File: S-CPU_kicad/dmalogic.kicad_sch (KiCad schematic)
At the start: 186 parts

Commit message: HDMA section seems correct after all. More notes added.
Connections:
- net ~{DMA_CHAN_RST} renamed ~{RESET_GDMA_CHAN_STOP_DMA_CHAN}
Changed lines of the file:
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@@
     (stroke (width 0) (type default))
   )
-  (wire (pts (xy 647.065 364.49) (xy 647.065 387.35))
+  (wire (pts (xy 647.065 367.665) (xy 647.065 387.35))
     (stroke (width 0) (type default))
   )
@@
     (stroke (width 0) (type default))
   )
-  (wire (pts (xy 475.615 364.49) (xy 647.065 364.49))
+  (wire (pts (xy 635.635 367.665) (xy 647.065 367.665))
     (stroke (width 0) (type default))
   )
@@
     (effects (font (size 1.27 1.27)) (justify right))
   )
-  (hierarchical_label "~{DMA_CHAN_RST}" (shape input) (at 254 44.45 180) (fields_autoplaced)
+  (hierarchical_label "~{RESET_GDMA_CHAN_STOP_DMA_CHAN}" (shape input) (at 254 44.45 180) (fields_autoplaced)
     (effects (font (size 1.27 1.27)) (justify right))
   )
@@
     (effects (font (size 1.27 1.27)) (justify right))
   )
-  (hierarchical_label "NEXT_CHAN_CLK" (shape input) (at 475.615 364.49 180) (fields_autoplaced)
+  (hierarchical_label "NEXT_CHAN_CLK" (shape input) (at 635.635 367.665 180) (fields_autoplaced)
     (effects (font (size 1.27 1.27)) (justify right))
   )

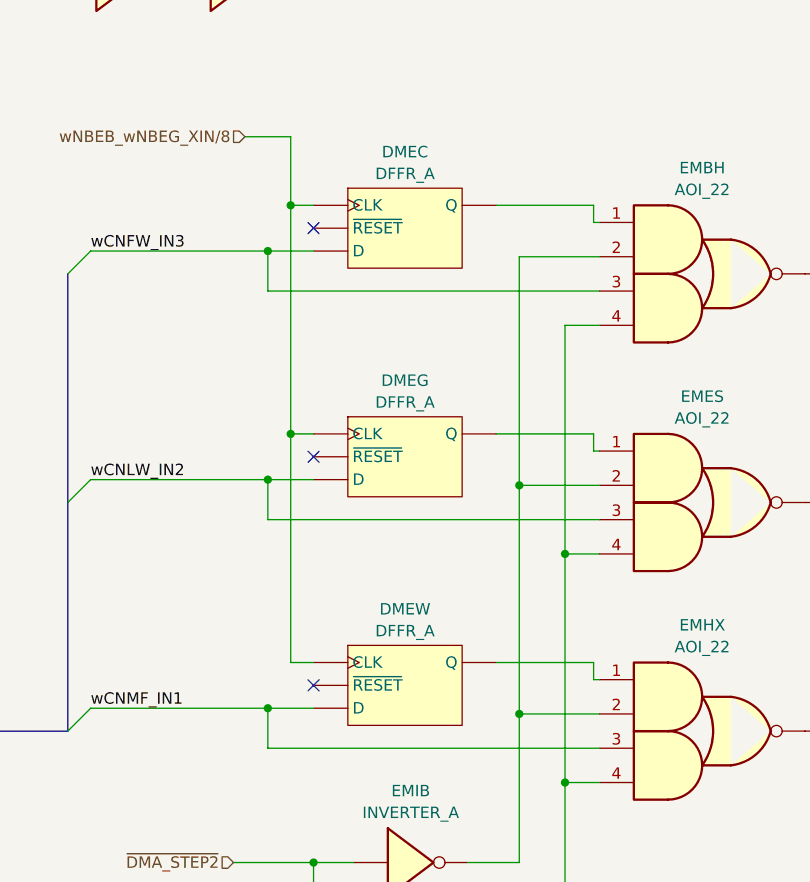
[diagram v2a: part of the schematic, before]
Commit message: Identified some DFFs as being DFFs with SET input rather than RESET input. It helps explaining a lot of beahiour in the MUL/DIV section and in the DMA section.
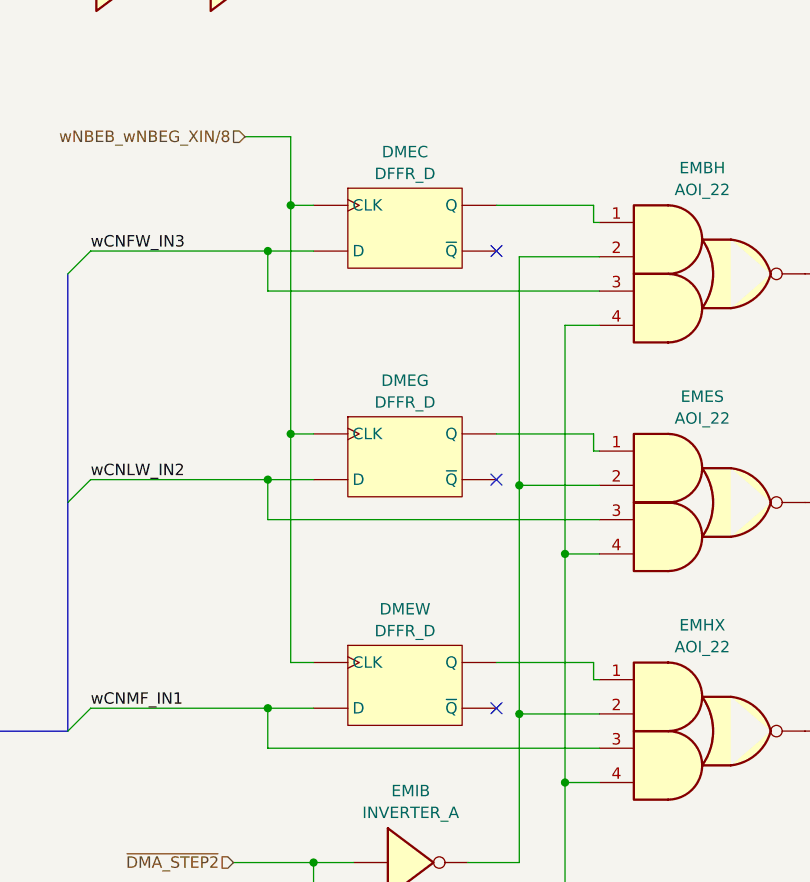
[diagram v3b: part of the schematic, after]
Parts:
- DMEC, DMEG, DMEW: value DFFR_A -> DFFR_D; symbol Ricoh_Cells:DFFR_A -> Ricoh_Cells:DFFR_D
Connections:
- net wNBEB_wNBEG_XIN/8: now also DMEC.1 (CLK), DMEG.1 (CLK), DMEW.1 (CLK); no longer DMEC.3 (CLK), DMEC.4 (~{CLK}), DMEG.3 (CLK), DMEG.4 (~{CLK}), DMEW.3 (CLK), DMEW.4 (~{CLK})
- net at EMES.1: now also DMEG.8 (Q); no longer DMEG.6 (Q)
- net at EMHX.1: now also DMEW.8 (Q); no longer DMEW.6 (Q)
- net at EMBH.1: now also DMEC.8 (Q); no longer DMEC.6 (Q)
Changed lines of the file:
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@@
   (no_connect (at 649.605 427.99))
   (no_connect (at 343.535 318.135))
-  (no_connect (at 732.79 427.99))
+  (no_connect (at 753.11 430.53))
   (no_connect (at 393.065 239.395))
   (no_connect (at 343.535 260.985))
   (no_connect (at 393.065 182.245))
-  (no_connect (at 732.79 453.39))
+  (no_connect (at 753.11 455.93))
   (no_connect (at 343.535 375.285))
   (no_connect (at 393.065 410.845))
@@
   (no_connect (at 649.605 389.89))
   (no_connect (at 343.535 432.435))
-  (no_connect (at 732.79 402.59))
+  (no_connect (at 753.11 405.13))
   (bus_entry (at 443.865 418.465) (size 2.54 2.54)
     (stroke (width 0) (type default))
@@
     )
   )
-  (symbol (lib_id "Ricoh_Cells:DFFR_A") (at 742.95 427.99 0) (unit 1)
+  (symbol (lib_id "Ricoh_Cells:DFFR_D") (at 742.95 427.99 0) (unit 1)
     (in_bom yes) (on_board yes) (dnp no) (fields_autoplaced)
     (property "Reference" "DMEG" (at 742.95 419.5277 0)
       (effects (font (size 1.27 1.27)))
     )
-    (property "Value" "DFFR_A" (at 742.95 421.9519 0)
+    (property "Value" "DFFR_D" (at 742.95 421.9519 0)
       (effects (font (size 1.27 1.27)))
     )
@@
       (effects (font (size 1.27 1.27)) hide)
     )
-    (property "Datasheet" "http://iceboy.a-singer.de/doc/dmg_cells.html#dffr_a" (at 742.95 436.245 0)
+    (property "Datasheet" "http://iceboy.a-singer.de/doc/dmg_cells.html#dffr_b" (at 742.95 436.245 0)
       (effects (font (size 1.27 1.27)) hide)
     )
     (pin "1")
     (pin "2")
-    (pin "3")
-    (pin "4")
-    (pin "5")
-    (pin "6")
+    (pin "7")
+    (pin "8")
     (instances
       (project "S-CPU"
@@
     )
   )
-  (symbol (lib_id "Ricoh_Cells:DFFR_A") (at 742.95 402.59 0) (unit 1)
+  (symbol (lib_id "Ricoh_Cells:DFFR_D") (at 742.95 402.59 0) (unit 1)
     (in_bom yes) (on_board yes) (dnp no) (fields_autoplaced)
     (property "Reference" "DMEC" (at 742.95 394.1277 0)
       (effects (font (size 1.27 1.27)))
     )
-    (property "Value" "DFFR_A" (at 742.95 396.5519 0)
+    (property "Value" "DFFR_D" (at 742.95 396.5519 0)
       (effects (font (size 1.27 1.27)))
     )
@@
       (effects (font (size 1.27 1.27)) hide)
     )
-    (property "Datasheet" "http://iceboy.a-singer.de/doc/dmg_cells.html#dffr_a" (at 742.95 410.845 0)
+    (property "Datasheet" "http://iceboy.a-singer.de/doc/dmg_cells.html#dffr_b" (at 742.95 410.845 0)
       (effects (font (size 1.27 1.27)) hide)
     )
     (pin "1")
     (pin "2")
-    (pin "3")
-    (pin "4")
-    (pin "5")
-    (pin "6")
+    (pin "7")
+    (pin "8")
     (instances
       (project "S-CPU"
@@
     )
   )
-  (symbol (lib_id "Ricoh_Cells:DFFR_A") (at 742.95 453.39 0) (unit 1)
+  (symbol (lib_id "Ricoh_Cells:DFFR_D") (at 742.95 453.39 0) (unit 1)
     (in_bom yes) (on_board yes) (dnp no) (fields_autoplaced)
     (property "Reference" "DMEW" (at 742.95 444.9277 0)
       (effects (font (size 1.27 1.27)))
     )
-    (property "Value" "DFFR_A" (at 742.95 447.3519 0)
+    (property "Value" "DFFR_D" (at 742.95 447.3519 0)
       (effects (font (size 1.27 1.27)))
     )
@@
       (effects (font (size 1.27 1.27)) hide)
     )
-    (property "Datasheet" "http://iceboy.a-singer.de/doc/dmg_cells.html#dffr_a" (at 742.95 461.645 0)
+    (property "Datasheet" "http://iceboy.a-singer.de/doc/dmg_cells.html#dffr_b" (at 742.95 461.645 0)
       (effects (font (size 1.27 1.27)) hide)
     )
     (pin "1")
     (pin "2")
-    (pin "3")
-    (pin "4")
-    (pin "5")
-    (pin "6")
+    (pin "7")
+    (pin "8")
     (instances
       (project "S-CPU"

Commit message: Fix ERC errors in schematics.
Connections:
- net wCNDH_~{EN} renamed DEMUX_~{EN}
- net wCNFW_IN3 renamed DEMUX_IN3
- net wCNLW_IN2 renamed DEMUX_IN2
- net wCNMF_IN1 renamed DEMUX_IN1
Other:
- title: SNES S-CPU Schematics  -> Reverse Engineered SNES S-CPU Schematics 
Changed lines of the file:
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@@
   (paper "A1")
   (title_block
-    (title "SNES S-CPU Schematics ")
+    (title "Reverse Engineered SNES S-CPU Schematics ")
     (date "2023-10-21")
     (rev "0.1")
@@
     (effects (font (size 1.27 1.27)) (justify left bottom))
   )
-  (label "wCNLW_IN2" (at 669.925 425.45 0) (fields_autoplaced)
+  (label "DEMUX_IN2" (at 669.925 425.45 0) (fields_autoplaced)
     (effects (font (size 1.27 1.27)) (justify left bottom))
   )
-  (label "wCNMF_IN1" (at 41.275 297.815 0) (fields_autoplaced)
+  (label "DEMUX_IN1" (at 41.275 297.815 0) (fields_autoplaced)
     (effects (font (size 1.27 1.27)) (justify left bottom))
   )
-  (label "wCNFW_IN3" (at 669.925 406.4 0) (fields_autoplaced)
+  (label "DEMUX_IN3" (at 669.925 406.4 0) (fields_autoplaced)
     (effects (font (size 1.27 1.27)) (justify left bottom))
   )
-  (label "wCNLW_IN2" (at 708.025 430.53 0) (fields_autoplaced)
+  (label "DEMUX_IN2" (at 708.025 430.53 0) (fields_autoplaced)
     (effects (font (size 1.27 1.27)) (justify left bottom))
   )
@@
     (effects (font (size 1.27 1.27)) (justify left bottom))
   )
-  (label "wCNDH_~{EN}" (at 669.925 387.35 0) (fields_autoplaced)
+  (label "DEMUX_~{EN}" (at 669.925 387.35 0) (fields_autoplaced)
     (effects (font (size 1.27 1.27)) (justify left bottom))
   )
@@
     (effects (font (size 1.27 1.27)) (justify left bottom))
   )
-  (label "wCNLW_IN2" (at 41.275 300.355 0) (fields_autoplaced)
+  (label "DEMUX_IN2" (at 41.275 300.355 0) (fields_autoplaced)
     (effects (font (size 1.27 1.27)) (justify left bottom))
   )
@@
     (effects (font (size 1.27 1.27)) (justify left bottom))
   )
-  (label "wCNDH_~{EN}" (at 41.275 310.515 0) (fields_autoplaced)
+  (label "DEMUX_~{EN}" (at 41.275 310.515 0) (fields_autoplaced)
     (effects (font (size 1.27 1.27)) (justify left bottom))
   )
@@
     (effects (font (size 1.27 1.27)) (justify left bottom))
   )
-  (label "wCNMF_IN1" (at 708.025 455.93 0) (fields_autoplaced)
+  (label "DEMUX_IN1" (at 708.025 455.93 0) (fields_autoplaced)
     (effects (font (size 1.27 1.27)) (justify left bottom))
   )
@@
     (effects (font (size 1.27 1.27)) (justify left bottom))
   )
-  (label "wCNFW_IN3" (at 708.025 405.13 0) (fields_autoplaced)
+  (label "DEMUX_IN3" (at 708.025 405.13 0) (fields_autoplaced)
     (effects (font (size 1.27 1.27)) (justify left bottom))
   )
@@
     (effects (font (size 1.27 1.27)) (justify left bottom))
   )
+  (label "DEMUX_IN[1..3]" (at 358.775 563.88 0) (fields_autoplaced)
+    (effects (font (size 1.27 1.27)) (justify left bottom))
+  )
   (label "420C_D0" (at 507.365 554.99 0) (fields_autoplaced)
     (effects (font (size 1.27 1.27)) (justify left bottom))
@@
     (effects (font (size 1.27 1.27)) (justify left bottom))
   )
-  (label "wCNFW_IN3" (at 41.275 302.895 0) (fields_autoplaced)
+  (label "DEMUX_IN3" (at 41.275 302.895 0) (fields_autoplaced)
     (effects (font (size 1.27 1.27)) (justify left bottom))
   )
@@
     (effects (font (size 1.27 1.27)) (justify right bottom))
   )
-  (label "wCNMF_IN1" (at 669.925 444.5 0) (fields_autoplaced)
+  (label "DEMUX_IN1" (at 669.925 444.5 0) (fields_autoplaced)
     (effects (font (size 1.27 1.27)) (justify left bottom))
   )
@@
         )
         (path "/ca9d3ca9-0297-4b98-a109-b7c162ccc5c3/6ab7ea20-bfb3-4f18-94ca-a294126fa0fb/606b397f-d353-4bdc-83fa-3e77f933e2b8"
-          (reference "UBNH") (unit 1)
+          (reference "OKJF") (unit 1)
         )
       )
@@
         )
         (path "/ca9d3ca9-0297-4b98-a109-b7c162ccc5c3/6ab7ea20-bfb3-4f18-94ca-a294126fa0fb/606b397f-d353-4bdc-83fa-3e77f933e2b8"
-          (reference "OKHF") (unit 1)
+          (reference "OKJL") (unit 1)
         )
       )
@@
         )
         (path "/ca9d3ca9-0297-4b98-a109-b7c162ccc5c3/6ab7ea20-bfb3-4f18-94ca-a294126fa0fb/606b397f-d353-4bdc-83fa-3e77f933e2b8"
-          (reference "OKHF") (unit 1)
+          (reference "OKIO") (unit 1)
         )
       )

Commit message: Big rework on the hierachical sheet to make thigs a bit clearer. PDF exported for Rev 0.1.
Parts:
- gave numbers to parts that had none: 2
- renumbered EBSG to CNDH, EBSG to CNFW, EBSG to CNLW, EBSG to CNMF, EBSG to HMAZ, EBVQ to HMBN, EBYP to HMDE, ECCU to HMDM, ECEK to HMEG, ECGN to HMFF, ECGO to HMJO, EBXE to HMRC, PAWC to LMAV, PAWC to LMGT, PAWC to LMSB, PAWC to LMXB, PAWC to LNGD, PAWC to LNLG, PAWC to LNOK, PAWC to LNXC, PAWC to MMBE, PAWC to MMMK, PAWC to MMQC, PAWC to MMVN, PAWC to MNFB, PAWC to MNLE, PAWC to MNRD, PAWC to MOEA, EBSG to NMAW, EBSG to NMBF, EBSG to NMCH, EBSG to NMGQ, EBSG to NMJJ, EBSG to NMJU, EBSG to NMLZ, EBSG to NMMX, UBNH to OKES, OKHF to OKIO, UBNH to OKJF, OKHF to OKJL
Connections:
- net 420B_D0: now also HMJO.9 (Q); no longer HMJO.7 (Q)
- net 420B_D1: now also HMFF.9 (Q); no longer HMFF.7 (Q)
- net 420B_D2: now also HMEG.9 (Q); no longer HMEG.7 (Q)
- net 420B_D3: now also HMDM.9 (Q); no longer HMDM.7 (Q)
- net 420B_D4: now also HMDE.9 (Q); no longer HMDE.7 (Q)
- net 420B_D5: now also HMRC.9 (Q); no longer HMRC.7 (Q)
- net 420B_D6: now also HMBN.9 (Q); no longer HMBN.7 (Q)
- net 420B_D7: now also HMAZ.9 (Q); no longer HMAZ.7 (Q)
- net DEMUX_IN1: now also CNMF.9 (Q); no longer CNMF.6 (Q)
- net DEMUX_IN2: now also CNLW.9 (Q); no longer CNLW.6 (Q)
- net DEMUX_IN3: now also CNFW.9 (Q); no longer CNFW.6 (Q)
- net DEMUX_~{EN}: now also CNDH.9 (Q); no longer CNDH.6 (Q)
- net NEXT_CHAN_CLK: now also CNDH.1 (CLK), CNFW.1 (CLK), CNLW.1 (CLK), CNMF.1 (CLK); no longer CNDH.3 (CLK), CNDH.4 (~{CLK}), CNFW.3 (CLK), CNFW.4 (~{CLK}), CNLW.3 (CLK), CNLW.4 (~{CLK}), CNMF.3 (CLK), CNMF.4 (~{CLK})
- net ~{420B_WR}: now also HMAZ.1 (CLK), HMBN.1 (CLK), HMDE.1 (CLK), HMDM.1 (CLK), HMEG.1 (CLK), HMFF.1 (CLK), HMJO.1 (CLK), HMRC.1 (CLK); no longer HMAZ.3 (CLK), HMAZ.4 (~{CLK}), HMBN.3 (CLK), HMBN.4 (~{CLK}), HMDE.3 (CLK), HMDE.4 (~{CLK}), HMDM.3 (CLK), HMDM.4 (~{CLK}), HMEG.3 (CLK), HMEG.4 (~{CLK}), HMFF.3 (CLK), HMFF.4 (~{CLK}), HMJO.3 (CLK), HMJO.4 (~{CLK}), HMRC.3 (CLK), HMRC.4 (~{CLK})
- net ~{420C_WR}: now also EBSG.1 (CLK), EBVQ.1 (CLK), EBXE.1 (CLK), EBYP.1 (CLK), ECCU.1 (CLK), ECEK.1 (CLK), ECGN.1 (CLK), ECGO.1 (CLK), JMBI.1 (CLK), JMBL.1 (CLK), JMCL.1 (CLK), JMGD.1 (CLK), JMIO.1 (CLK), JMIY.1 (CLK), JMJE.1 (CLK), JMKG.1 (CLK); no longer EBSG.3 (CLK), EBSG.4 (~{CLK}), EBVQ.3 (CLK), EBVQ.4 (~{CLK}), EBXE.3 (CLK), EBXE.4 (~{CLK}), EBYP.3 (CLK), EBYP.4 (~{CLK}), ECCU.3 (CLK), ECCU.4 (~{CLK}), ECEK.3 (CLK), ECEK.4 (~{CLK}), ECGN.3 (CLK), ECGN.4 (~{CLK}), ECGO.3 (CLK), ECGO.4 (~{CLK}), JMBI.3 (CLK), JMBI.4 (~{CLK}), JMBL.3 (CLK), JMBL.4 (~{CLK}), JMCL.3 (CLK), JMCL.4 (~{CLK}), JMGD.3 (CLK), JMGD.4 (~{CLK}), JMIO.3 (CLK), JMIO.4 (~{CLK}), JMIY.3 (CLK), JMIY.4 (~{CLK}), JMJE.3 (CLK), JMJE.4 (~{CLK}), JMKG.3 (CLK), JMKG.4 (~{CLK})
- net ~{RESTART_DMA}: now also FMCD.6 (~{RESET}), FMFF.6 (~{RESET}), FMGC.6 (~{RESET}), FMHJ.6 (~{RESET}), FMHZ.6 (~{RESET}), FMKL.6 (~{RESET}), FMUY.6 (~{RESET}), FMWM.6 (~{RESET}); no longer FMCD.1 (~{RESET}), FMCD.5 (~{RESET}), FMFF.1 (~{RESET}), FMFF.5 (~{RESET}), FMGC.1 (~{RESET}), FMGC.5 (~{RESET}), FMHJ.1 (~{RESET}), FMHJ.5 (~{RESET}), FMHZ.1 (~{RESET}), FMHZ.5 (~{RESET}), FMKL.1 (~{RESET}), FMKL.5 (~{RESET}), FMUY.1 (~{RESET}), FMUY.5 (~{RESET}), FMWM.1 (~{RESET}), FMWM.5 (~{RESET})
- net at LMUV.2, MNPG.2: now also NMGQ.9 (Q); no longer NMGQ.6 (Q)
- net at LNKU.2, MNJI.2: now also NMJU.9 (Q); no longer NMJU.6 (Q)
- net at DMHY.1: now also FMGC.8 (~{Q}); no longer FMGC.6 (~{Q})
- net at HMBN.6 (~{RESET}): now also GMNY.3
- net at KMAZ.1: now also JMBI.9 (Q); no longer JMBI.6 (Q)
- net at HMJO.6 (~{RESET}): now also GNQI.3
- net at KMGA.1: now also JMGD.9 (Q); no longer JMGD.6 (Q)
- net at DBZJ.1: now also ECGO.9 (Q); no longer ECGO.6 (Q)
- net at DBZJ.2: now also ECGN.9 (Q); no longer ECGN.6 (Q)
- net at DBZJ.3: now also ECEK.9 (Q); no longer ECEK.6 (Q)
- net at DBZJ.4: now also ECCU.9 (Q); no longer ECCU.6 (Q)
- net at DNBO.2: now also FMHZ.8 (~{Q}); no longer FMHZ.6 (~{Q})
- net at LMFY.1, MMLQ.1: now also NMBF.9 (Q); no longer NMBF.6 (Q)
- net at CMCO.1: now also FMCD.8 (~{Q}); no longer FMCD.6 (~{Q})
- net at LMFG.1, MNHE.1: now also NMAW.9 (Q); no longer NMAW.6 (Q)
- net at HMAZ.6 (~{RESET}): now also GMEX.3
- net at KMQC.1: now also JMIY.9 (Q); no longer JMIY.6 (Q)
- net at HMRC.6 (~{RESET}): now also GMSH.3
- net at DNBU.1: now also FMKL.8 (~{Q}); no longer FMKL.6 (~{Q})
- net at DNBY.1: now also FMUY.8 (~{Q}); no longer FMUY.6 (~{Q})
- net at KMEU.1: now also JMCL.9 (Q); no longer JMCL.6 (Q)
- net at HMDE.6 (~{RESET}): now also GMVF.3
- net at LMPF.2, MNOG.2: now also NMCH.9 (Q); no longer NMCH.6 (Q)
- net at KMVO.1: now also JMKG.9 (Q); no longer JMKG.6 (Q)
- net at LNHX.1, MNHM.1: now also NMJJ.9 (Q); no longer NMJJ.6 (Q)
- net at HMEG.6 (~{RESET}): now also GNCF.3
- net at DBWG.3: now also EBVQ.9 (Q); no longer EBVQ.6 (Q)
- net at DBWG.1: now also EBYP.9 (Q); no longer EBYP.6 (Q)
- net at LNNE.2, MNNS.2: now also NMLZ.9 (Q); no longer NMLZ.6 (Q)
- net at CMEU.1: now also FMFF.8 (~{Q}); no longer FMFF.6 (~{Q})
- net at KMCA.1: now also JMBL.9 (Q); no longer JMBL.6 (Q)
- net at HMDM.6 (~{RESET}): now also GNBN.3
- net at DMPK.1: now also FMHJ.8 (~{Q}); no longer FMHJ.6 (~{Q})
- net at KMSG.1: now also JMJE.9 (Q); no longer JMJE.6 (Q)
- net at KMHW.2: now also JMIO.9 (Q); no longer JMIO.6 (Q)
- net at DBWG.2: now also EBXE.9 (Q); no longer EBXE.6 (Q)
- net at DBWG.4: now also EBSG.9 (Q); no longer EBSG.6 (Q)
- net at HMFF.6 (~{RESET}): now also GNKJ.3
- net at LNTA.1, MOBP.1: now also NMMX.9 (Q); no longer NMMX.6 (Q)
- net at EMPN.1: now also FMWM.8 (~{Q}); no longer FMWM.6 (~{Q})
- removed net wDBJW_wHASI_~{RST}: EBSG.1 (~{RESET}), EBSG.5 (~{RESET}), EBVQ.1 (~{RESET}), EBVQ.5 (~{RESET}), EBXE.1 (~{RESET}), EBXE.5 (~{RESET}), EBYP.1 (~{RESET}), EBYP.5 (~{RESET}), ECCU.1 (~{RESET}), ECCU.5 (~{RESET}), ECEK.1 (~{RESET}), ECEK.5 (~{RESET}), ECGN.1 (~{RESET}), ECGN.5 (~{RESET}), ECGO.1 (~{RESET}), ECGO.5 (~{RESET}), GMEX.2, GMNY.2, GMSH.2, GMVF.2, GNBN.2, GNCF.2, GNKJ.2, GNQI.2, JMBI.1 (~{RESET}), JMBI.5 (~{RESET}), JMBL.1 (~{RESET}), JMBL.5 (~{RESET}), JMCL.1 (~{RESET}), JMCL.5 (~{RESET}), JMGD.1 (~{RESET}), JMGD.5 (~{RESET}), JMIO.1 (~{RESET}), JMIO.5 (~{RESET}), JMIY.1 (~{RESET}), JMIY.5 (~{RESET}), JMJE.1 (~{RESET}), JMJE.5 (~{RESET}), JMKG.1 (~{RESET}), JMKG.5 (~{RESET})
- removed net wNBEB_wNBEG_XIN/8: DMEC.1 (CLK), DMEG.1 (CLK), DMEW.1 (CLK), NMAW.3 (CLK), NMAW.4 (~{CLK}), NMBF.3 (CLK), NMBF.4 (~{CLK}), NMCH.3 (CLK), NMCH.4 (~{CLK}), NMGQ.3 (CLK), NMGQ.4 (~{CLK}), NMJJ.3 (CLK), NMJJ.4 (~{CLK}), NMJU.3 (CLK), NMJU.4 (~{CLK}), NMLZ.3 (CLK), NMLZ.4 (~{CLK}), NMMX.3 (CLK), NMMX.4 (~{CLK})
- new net: FMGC.1 (CLK), GMTW.2
- new net: FMUY.1 (CLK), GNOJ.2
- new net: FMHZ.1 (CLK), GNBQ.2
- new net: NMAW.6 (~{RESET}), NMBF.6 (~{RESET}), NMCH.6 (~{RESET}), NMGQ.6 (~{RESET}), NMJJ.6 (~{RESET}), NMJU.6 (~{RESET}), NMLZ.6 (~{RESET}), NMMX.6 (~{RESET}), NMTQ.2
- new net: FMCD.1 (CLK), GMIV.2
- new net: FMKL.1 (CLK), GNIU.2
- new net: FMWM.1 (CLK), GNSB.2
- new net: FMHJ.1 (CLK), GMXT.2
- new net: FMFF.1 (CLK), GMOL.2
- new net DMA_XIN/8: DMEC.1 (CLK), DMEG.1 (CLK), DMEW.1 (CLK), NMAW.1 (CLK), NMBF.1 (CLK), NMCH.1 (CLK), NMGQ.1 (CLK), NMJJ.1 (CLK), NMJU.1 (CLK), NMLZ.1 (CLK), NMMX.1 (CLK)
- new net ~{MRST}: EBSG.6 (~{RESET}), EBVQ.6 (~{RESET}), EBXE.6 (~{RESET}), EBYP.6 (~{RESET}), ECCU.6 (~{RESET}), ECEK.6 (~{RESET}), ECGN.6 (~{RESET}), ECGO.6 (~{RESET}), GMEX.2, GMNY.2, GMSH.2, GMVF.2, GNBN.2, GNCF.2, GNKJ.2, GNQI.2, JMBI.6 (~{RESET}), JMBL.6 (~{RESET}), JMCL.6 (~{RESET}), JMGD.6 (~{RESET}), JMIO.6 (~{RESET}), JMIY.6 (~{RESET}), JMJE.6 (~{RESET}), JMKG.6 (~{RESET})

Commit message: Fixed VAWR which should have been an SR DFF (to fix issue #3 raised in github)
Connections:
- net +5V: now also EMIZ.6 (E3); no longer EMIZ. (~{OUT7})
- net DEMUX_IN1: now also EMIZ.1 (IN1); no longer EMIZ. (~{OUT7})
- net DEMUX_IN2: now also EMIZ.2 (IN2); no longer EMIZ. (~{OUT7})
- net DEMUX_IN3: now also EMIZ.3 (IN3); no longer EMIZ. (~{OUT7})
- net DEMUX_~{EN}: now also EMIZ.4 (~{E1}), EMIZ.5 (~{E2}); no longer EMIZ. (~{OUT7})
- net at GMYD.2, NMGQ.2 (D): now also EMIZ.10 (~{OUT3}); no longer EMIZ. (~{OUT7})
- net at EMAU.1: now also EMBH.5; no longer EMBH.3
- net at EMGX.1: now also EMHX.5; no longer EMHX.3
- net at EMCQ.1: now also EMES.5; no longer EMES.3
- net at GMNG.2, NMAW.2 (D): now also EMIZ.7 (~{OUT0}); no longer EMIZ. (~{OUT7})
- net at GNSN.2, NMMX.2 (D): now also EMIZ.15 (~{OUT7}); no longer EMIZ. (~{OUT7})
- net at GMUF.2, NMCH.2 (D): now also EMIZ.9 (~{OUT2}); no longer EMIZ. (~{OUT7})
- net at GNIX.2, NMJU.2 (D): now also EMIZ.12 (~{OUT5}); no longer EMIZ. (~{OUT7})
- net at GNBU.2, NMJJ.2 (D): now also EMIZ.11 (~{OUT4}); no longer EMIZ. (~{OUT7})
- net at GNPC.2, NMLZ.2 (D): now also EMIZ.13 (~{OUT6}); no longer EMIZ. (~{OUT7})
- net at GMOP.2, NMBF.2 (D): now also EMIZ.8 (~{OUT1}); no longer EMIZ. (~{OUT7})
- net DISABLE_HDMA_CHANNEL renamed PAUSE_HDMA_CHAN
- net HDMA_CHAN_RST renamed STOP_HDMA_CHAN
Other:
- note added: "ADDRESS DECODING"
- moved on the sheet: CMCO, CMER, CMEU, CMKK, CMOY, CNDH, CNFW, CNLW, CNMF, CNNO, CNRJ, CNRU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
